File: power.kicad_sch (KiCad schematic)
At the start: 48 parts, among them Q1 CSD23203W, Q2 BC846BPDW1, Q3 BC846BPDW1, U4 TPSM828212SILR, U5 TPSM828214SILR, U6 LM66100DCK, U7 TPS7A94, U8 TPS7A0512PDBV, U9 LT1054

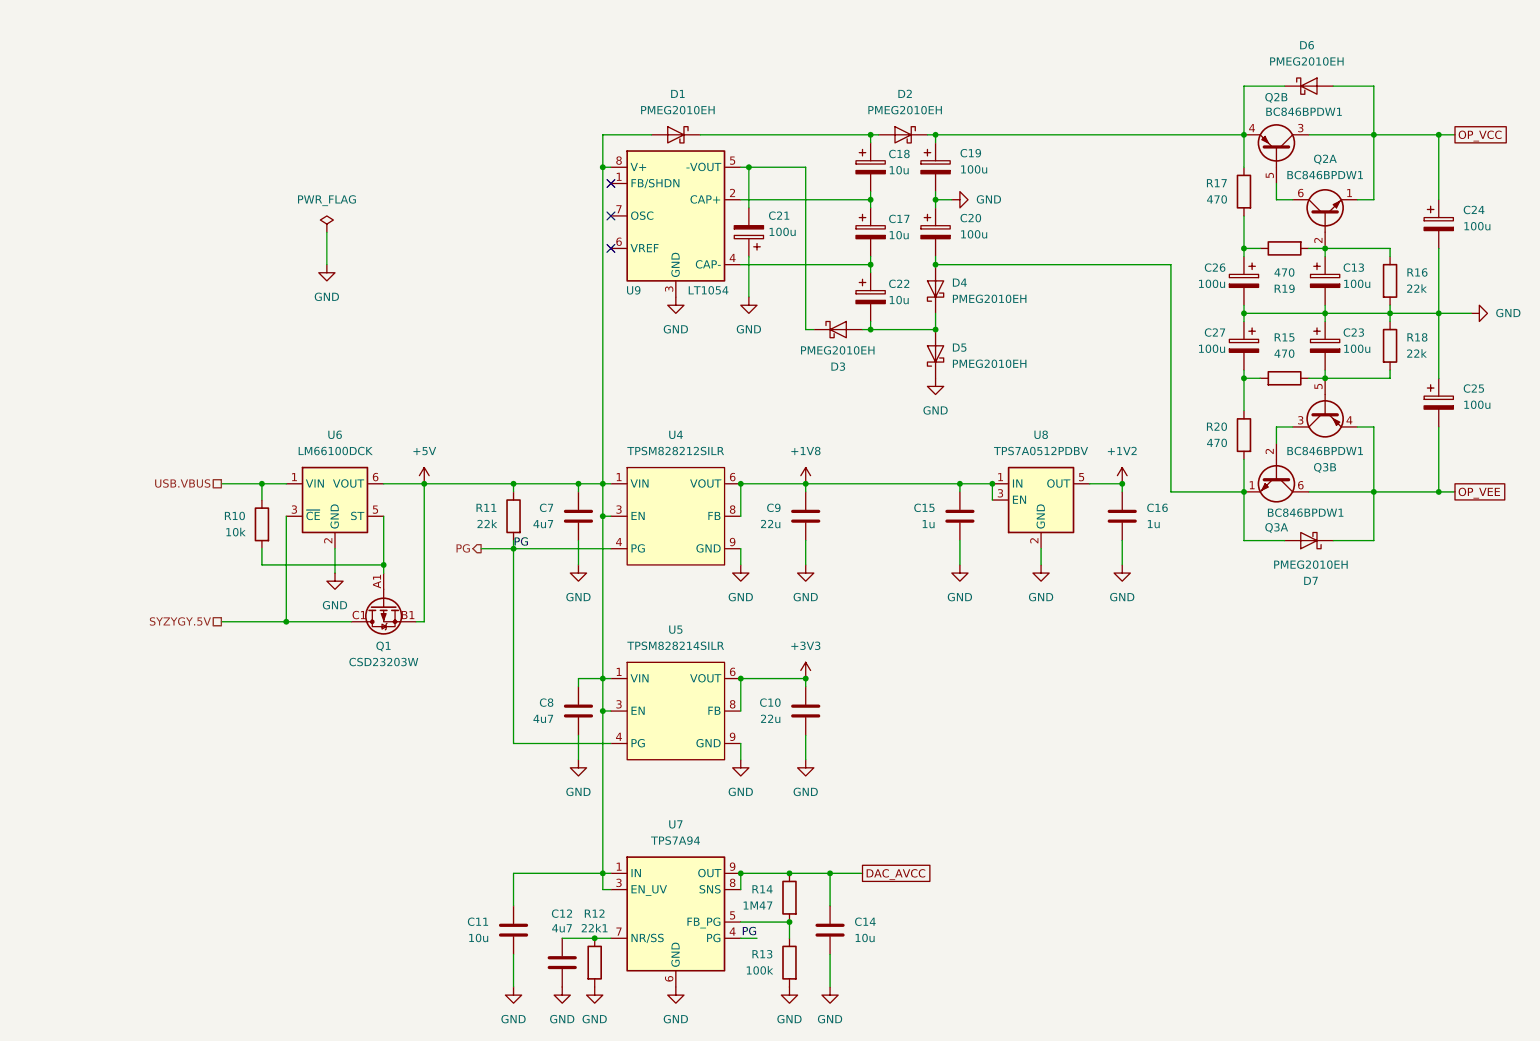
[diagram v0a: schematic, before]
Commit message: Converted connector power to global labels
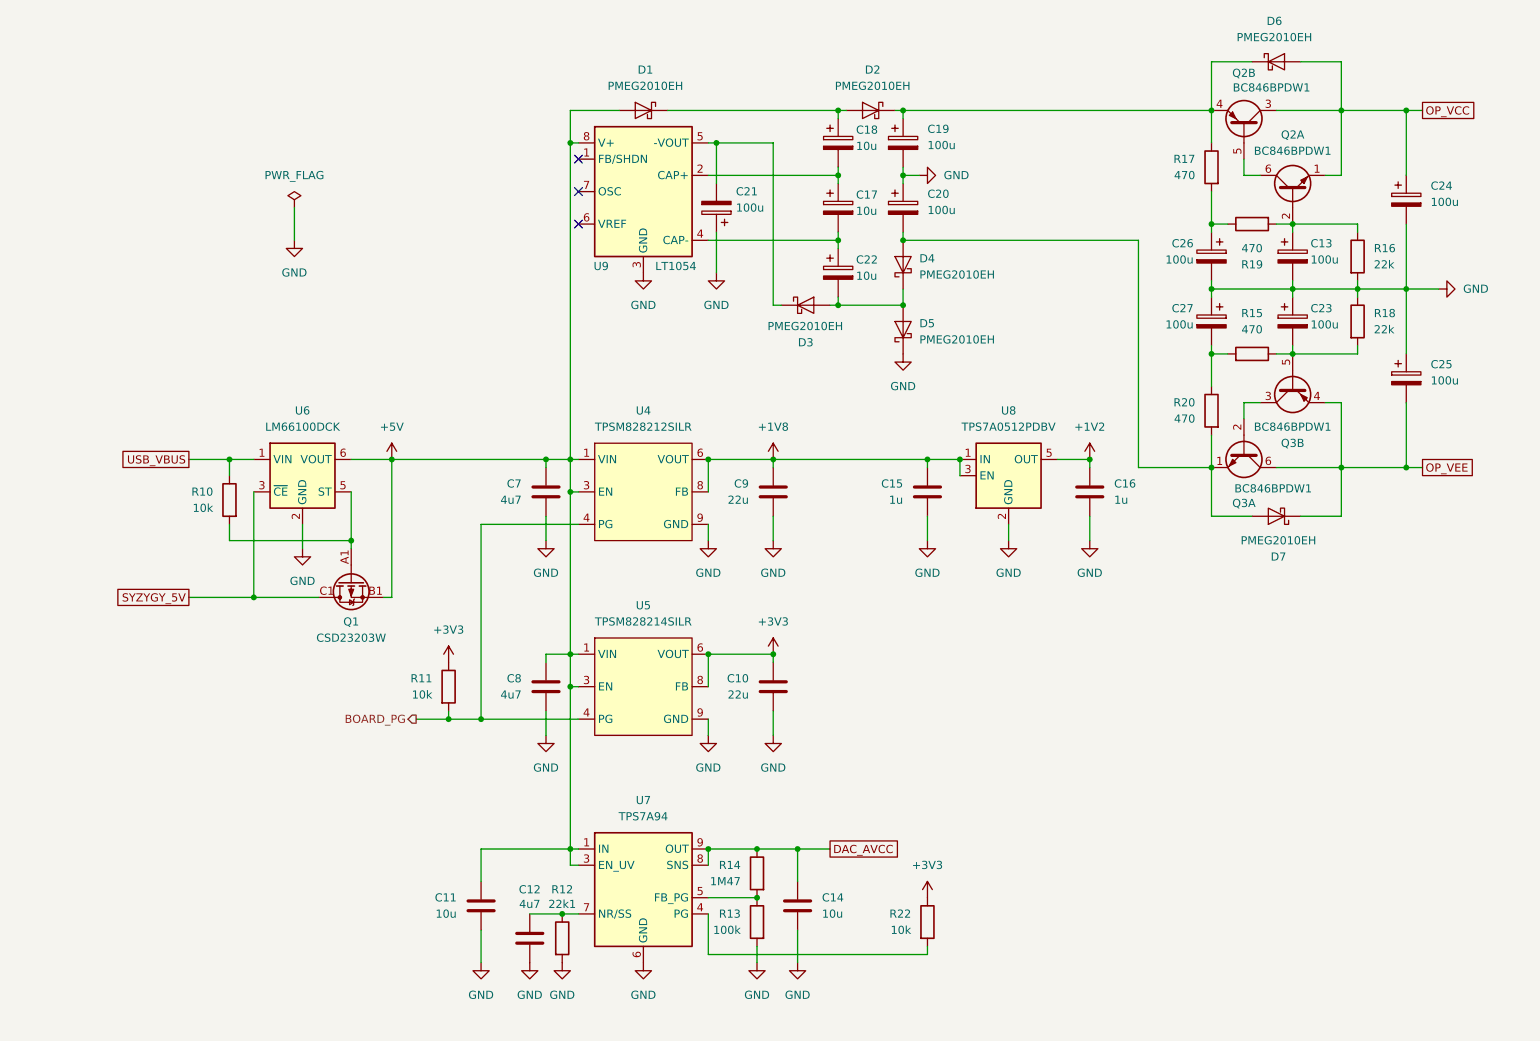
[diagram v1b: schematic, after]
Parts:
- added R22: 10k, symbol Device:R
- R11: value 22k -> 10k
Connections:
- net +3V3: now also R11.1, R22.1
- net +5V: no longer R11.1
- net PG renamed BOARD_PG
- net BOARD_PG: no longer U7.4 (PG)
- net SYZYGY.5V renamed SYZYGY_5V
- net USB.VBUS renamed USB_VBUS
- new net: R22.2, U7.4 (PG)
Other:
- moved on the sheet: C10, C11, C12, C13, C14, C15, C16, C17, C18, C19, C20, C21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

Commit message: Added pMCU
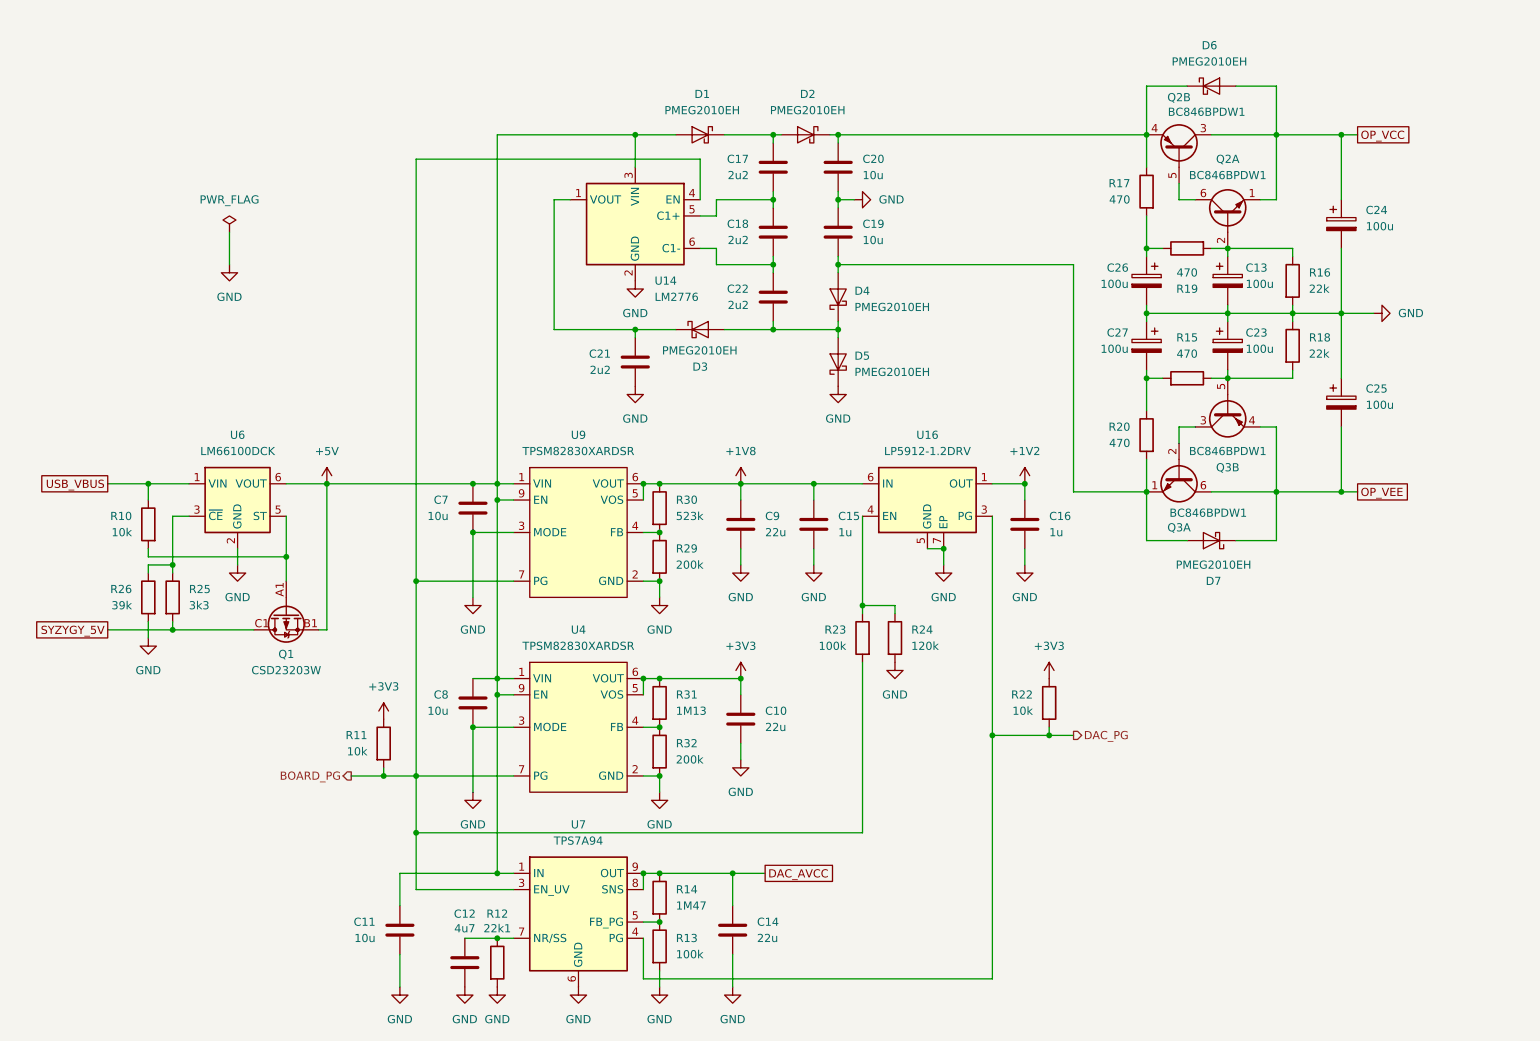
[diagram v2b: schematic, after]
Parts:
- removed C17, C18, C22: 10u, symbol Device:C_Polarized
- removed C19, C20, C21: 100u, symbol Device:C_Polarized
- removed U4: TPSM828212SILR, lib_fp:uSIP-10, symbol albert-custom:TPSM8282XSILR
- removed U5: TPSM828214SILR, lib_fp:uSIP-10, symbol albert-custom:TPSM8282XSILR
- removed U8: TPS7A0512PDBV, Package_TO_SOT_SMD:SOT-23-5, symbol Regulator_Linear:TPS7A0512PDBV
- removed U9: LT1054, symbol Regulator_SwitchedCapacitor:LT1054
- added C17, C18, C21, C22: 2u2, symbol Device:C
- added C19, C20: 10u, symbol Device:C
- added R23: 100k, symbol Device:R
- added R24: 120k, symbol Device:R
- added R25: 3k3, symbol Device:R
- added R26: 39k, symbol Device:R
- added R29, R32: 200k, symbol Device:R
- added R30: 523k, symbol Device:R
- added R31: 1M13, symbol Device:R
- added U14: LM2776, Package_TO_SOT_SMD:SOT-23-6, symbol Regulator_SwitchedCapacitor:LM2776
- added U16: LP5912-1.2DRV, Package_SON:WSON-6-1EP_2x2mm_P0.65mm_EP1x1.6mm_ThermalVias, symbol Regulator_Linear:LP5912-1.2DRV
- added U4, U9: TPSM82830XARDSR, lib_fp:QFN-FCMOD-RDS0009A, symbol albert-custom:TPSM82830XARDSR
- C14: value 10u -> 22u
- C7, C8: value 4u7 -> 10u
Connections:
- net +1V2: now also U16.1 (OUT)
- net +1V8: now also R30.1, U16.6 (IN), U9.5 (VOS), U9.6 (VOUT)
- net +3V3: now also R31.1, U4.5 (VOS), U4.6 (VOUT)
- net +5V: now also U14.3 (VIN), U4.1 (VIN), U4.9 (EN), U9.1 (VIN), U9.9 (EN); no longer U7.3 (EN_UV)
- net BOARD_PG: now also U7.3 (EN_UV), R23.2, U14.4 (EN), U4.7 (PG), U9.7 (PG)
- net GND: now also C19.1, C20.2, C21.2, R24.2, R26.2, R29.2, R32.2, U14.2 (GND), U16.5 (GND), U16.7 (EP), U4.2 (GND), U4.3 (MODE), U9.2 (GND), U9.3 (MODE)
- net SYZYGY_5V: now also R25.2; no longer U6.3 (~{CE})
- net at D3.1 (K): now also C21.1, U14.1 (VOUT)
- net at D3.2 (A), D4.1 (K), D5.2 (A): now also C22.2
- net at D2.1 (K), D6.1 (K), Q2.4 (E2)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: now also C20.1
- net at D4.2 (A), D7.2 (A), Q3.1 (E1)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: now also C19.2
- net DAC_PG: now reaches R22.2, U7.4 (PG)
- net DAC_PG: now also U16.3 (PG)
- net at D1.1 (K), D2.2 (A): now also C17.1
- new net: C18.2, C22.1, U14.6 (C1-)
- new net: R29.1, R30.2, U9.4 (FB)
- new net: C17.2, C18.1, U14.5 (C1+)
- new net: R25.1, R26.1, U6.3 (~{CE})
- new net: R23.1, R24.1, U16.4 (EN)
- new net: R31.2, R32.1, U4.4 (FB)
- no-connect marks 3 -> 0
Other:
- moved on the sheet: C10, C11, C12, C13, C14, C15, C16, C23, C24, C25, C26, C27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
